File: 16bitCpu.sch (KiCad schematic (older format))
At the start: 0 parts

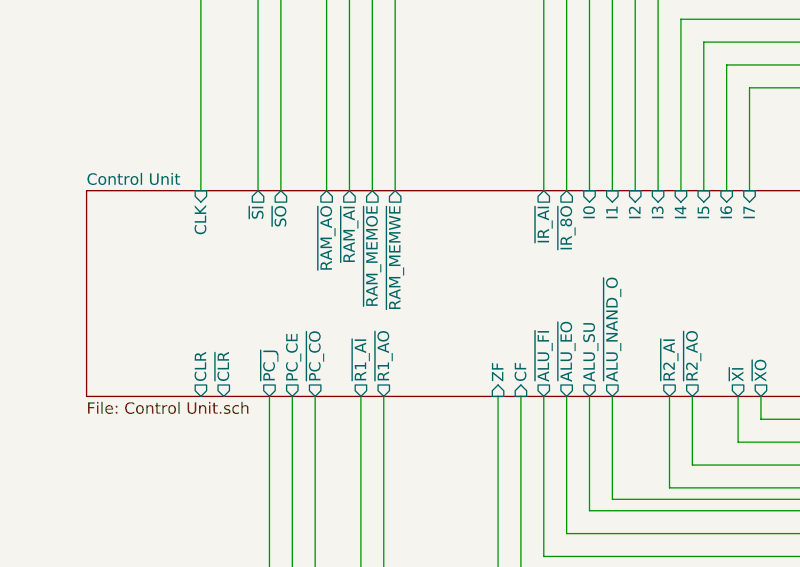
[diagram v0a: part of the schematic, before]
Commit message: using new RAM and ROM,15bits baby
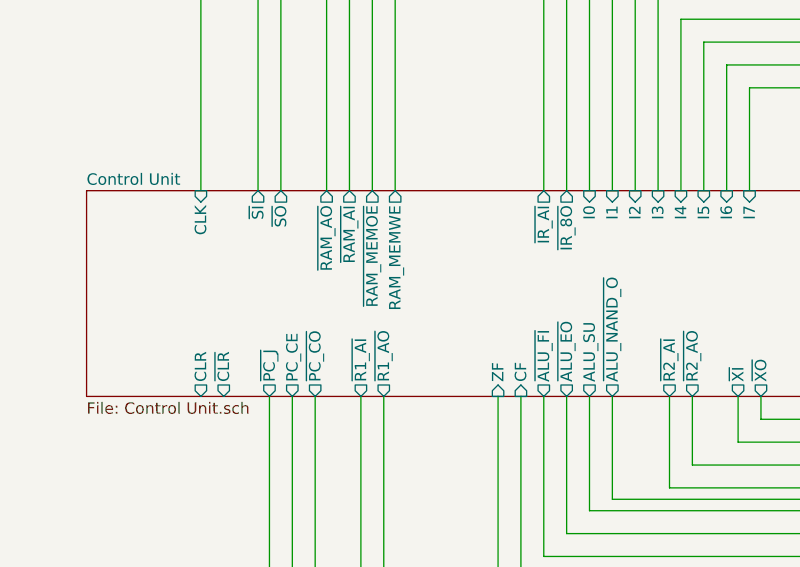
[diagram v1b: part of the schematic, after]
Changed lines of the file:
@@
 F21 "~RAM_AO" O T 1950 12300 50
 F22 "~RAM_MEMOE" O T 2150 12300 50
-F23 "~RAM_MEMWE" O T 2250 12300 50
-F24 "~IR_AI" O T 2900 12300 50
-F25 "~PC_J" O B 1700 13200 50
-F26 "PC_CE" O B 1800 13200 50
-F27 "~PC_CO" O B 1900 13200 50
-F28 "CLR" O B 1400 13200 50
-F29 "~CLR" O B 1500 13200 50
-F30 "~SI" O T 1650 12300 50
-F31 "~SO" O T 1750 12300 50
-F32 "~XI" O B 3750 13200 50
-F33 "~XO" O B 3850 13200 50
-F34 "~IR_8O" O T 3000 12300 50
-F35 "~ALU_NAND_O" O B 3200 13200 50
+F23 "~IR_AI" O T 2900 12300 50
+F24 "~PC_J" O B 1700 13200 50
+F25 "PC_CE" O B 1800 13200 50
+F26 "~PC_CO" O B 1900 13200 50
+F27 "CLR" O B 1400 13200 50
+F28 "~CLR" O B 1500 13200 50
+F29 "~SI" O T 1650 12300 50
+F30 "~SO" O T 1750 12300 50
+F31 "~XI" O B 3750 13200 50
+F32 "~XO" O B 3850 13200 50
+F33 "~IR_8O" O T 3000 12300 50
+F34 "~ALU_NAND_O" O B 3200 13200 50
+F35 "RAM_MEMWE" O T 2250 12300 50
 $EndSheet
 $Sheet

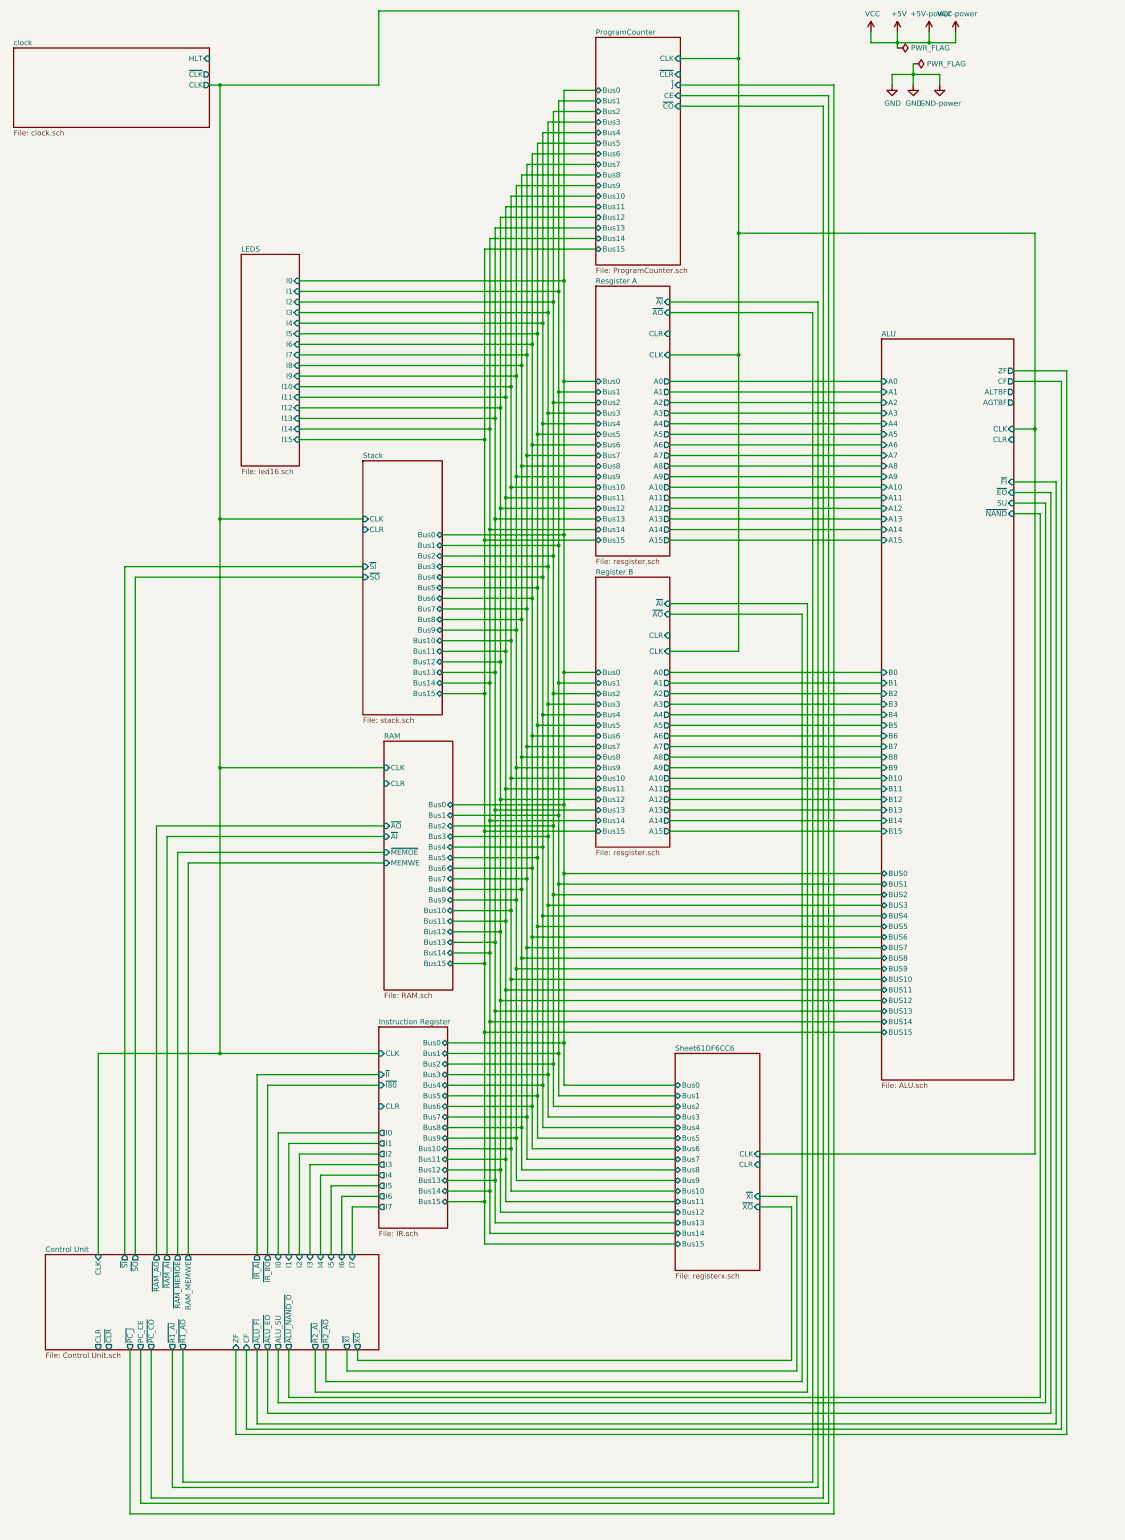
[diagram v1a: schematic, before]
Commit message: using new ROM in CU and more jumps
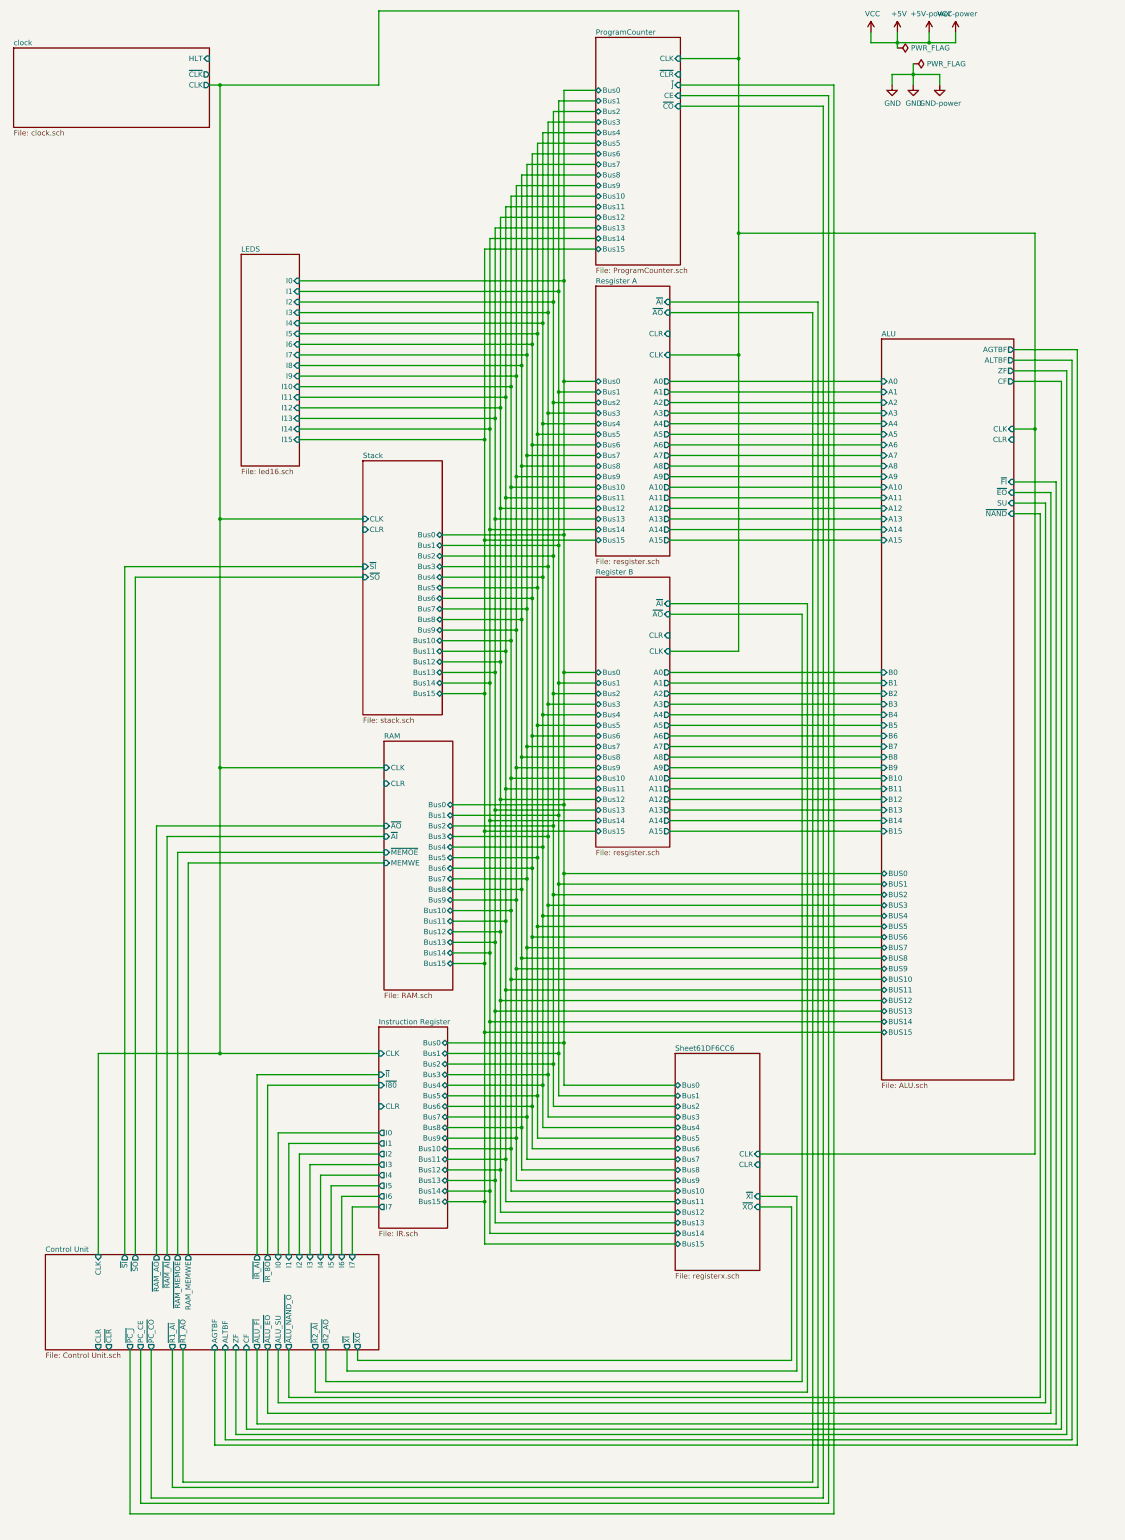
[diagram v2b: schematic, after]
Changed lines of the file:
@@
 F34 "~ALU_NAND_O" O B 3200 13200 50
 F35 "RAM_MEMWE" O T 2250 12300 50
+F36 "ALTBF" I B 2600 13200 50
+F37 "AGTBF" I B 2500 13200 50
 $EndSheet
 $Sheet
@@
 F55 "CF" O R 10050 4050 50
 F56 "ZF" O R 10050 3950 50
-F57 "ALTBF" O R 10050 4150 50
-F58 "AGTBF" O R 10050 4250 50
+F57 "ALTBF" O R 10050 3850 50
+F58 "AGTBF" O R 10050 3750 50
 F59 "~NAND" I R 10050 5300 50
 $EndSheet
@@
 Wire Wire Line
 	3200 13650 3200 13200
+Wire Wire Line
+	2600 13200 2600 14050
+Wire Wire Line
+	2600 14050 10600 14050
+Wire Wire Line
+	10600 14050 10600 3850
+Wire Wire Line
+	10600 3850 10050 3850
+Wire Wire Line
+	10050 3750 10650 3750
+Wire Wire Line
+	10650 3750 10650 14100
+Wire Wire Line
+	10650 14100 2500 14100
+Wire Wire Line
+	2500 14100 2500 13200
 $EndSCHEMATC

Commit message: fixed almost all errors
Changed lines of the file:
@@
 Wire Wire Line
 	7450 2650 10250 2650
-Wire Wire Line
-	10250 2650 10250 4500
 Connection ~ 7450 2650
 Wire Wire Line
@@
 Wire Wire Line
 	2500 14100 2500 13200
+Wire Wire Line
+	1400 13200 1400 14900
+Wire Wire Line
+	1400 14900 11000 14900
+Wire Wire Line
+	11000 4600 10050 4600
+Wire Wire Line
+	11000 1950 8500 1950
+Wire Wire Line
+	8500 1950 8500 1150
+Wire Wire Line
+	8500 1150 6900 1150
+Connection ~ 11000 4600
+Wire Wire Line
+	6800 6450 11000 6450
+Connection ~ 11000 6450
+Wire Wire Line
+	11000 6450 11000 4600
+Wire Wire Line
+	7650 11450 11000 11450
+Wire Wire Line
+	11000 6450 11000 11450
+Connection ~ 11000 11450
+Wire Wire Line
+	11000 11450 11000 14900
+Wire Wire Line
+	10250 2650 10250 4500
+Wire Wire Line
+	6800 3600 11000 3600
+Wire Wire Line
+	11000 1950 11000 3600
+Connection ~ 11000 3600
+Wire Wire Line
+	11000 3600 11000 4600
+Wire Wire Line
+	1400 14900 650  14900
+Wire Wire Line
+	650  5450 3900 5450
+Connection ~ 1400 14900
+Wire Wire Line
+	4100 7850 650  7850
+Connection ~ 650  7850
+Wire Wire Line
+	650  7850 650  5450
+Wire Wire Line
+	4050 10900 650  10900
+Wire Wire Line
+	650  7850 650  10900
+Connection ~ 650  10900
+Wire Wire Line
+	650  10900 650  14900
 $EndSCHEMATC

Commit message: fixed more errors
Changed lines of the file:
@@
 	8950 750  8950 850
-$Comp
-L 16bitCpu-rescue:PWR_FLAG-power #FLG01
-U 1 1 6041ADF9
-P 8950 900
-F 0 "#FLG01" H 8950 975 50  0001 C CNN
-F 1 "PWR_FLAG" V 8950 1028 50  0000 L CNN
-F 2 "" H 8950 900 50  0001 C CNN
-F 3 "~" H 8950 900 50  0001 C CNN
-	1    8950 900
-	0    1    1    0
-$EndComp
-$Comp
-L 16bitCpu-rescue:PWR_FLAG-power #FLG02
-U 1 1 6041B51D
-P 9100 1050
-F 0 "#FLG02" H 9100 1125 50  0001 C CNN
-F 1 "PWR_FLAG" V 9100 1178 50  0000 L CNN
-F 2 "" H 9100 1050 50  0001 C CNN
-F 3 "~" H 9100 1050 50  0001 C CNN
-	1    9100 1050
-	0    1    1    0
-$EndComp
 $Comp
 L 16bitCpu-rescue:GND-power #PWR04
@@
 	1    0    0    -1
 $EndComp
-Wire Wire Line
-	9100 1050 9100 1150
 $Comp
 L 16bitCpu-rescue:GND-power #PWR02
@@
 	8700 850  8950 850
 Connection ~ 8950 850
-Wire Wire Line
-	8950 850  8950 900
 $Sheet
 S 900  12300 3150 900

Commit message: added images,fixed readme,renamed stuff to not include spaces
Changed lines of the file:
@@
 S 6100 3150 700  2550
 U 5F67C726
-F0 "Resgister A" 50
+F0 "Resgister-A" 50
 F1 "resgister.sch" 50
 F2 "CLK" I R 6800 3800 50
@@
 S 6100 5900 700  2550
 U 5F74778C
-F0 "Register B" 50
+F0 "Register-B" 50
 F1 "resgister.sch" 50
 F2 "CLK" I R 6800 6600 50
@@
 Connection ~ 8950 850
 $Sheet
-S 900  12300 3150 900
-U 5FD099BF
-F0 "Control Unit" 50
-F1 "Control Unit.sch" 50
-F2 "I1" I T 3200 12300 50
-F3 "I0" I T 3100 12300 50
-F4 "I2" I T 3300 12300 50
-F5 "I3" I T 3400 12300 50
-F6 "I4" I T 3500 12300 50
-F7 "I5" I T 3600 12300 50
-F8 "I6" I T 3700 12300 50
-F9 "I7" I T 3800 12300 50
-F10 "CLK" I T 1400 12300 50
-F11 "ZF" I B 2700 13200 50
-F12 "CF" I B 2800 13200 50
-F13 "~ALU_FI" O B 2900 13200 50
-F14 "ALU_SU" O B 3100 13200 50
-F15 "~ALU_EO" O B 3000 13200 50
-F16 "~R1_AI" O B 2100 13200 50
-F17 "~R1_AO" O B 2200 13200 50
-F18 "~R2_AI" O B 3450 13200 50
-F19 "~R2_AO" O B 3550 13200 50
-F20 "~RAM_AI" O T 2050 12300 50
-F21 "~RAM_AO" O T 1950 12300 50
-F22 "~RAM_MEMOE" O T 2150 12300 50
-F23 "~IR_AI" O T 2900 12300 50
-F24 "~PC_J" O B 1700 13200 50
-F25 "PC_CE" O B 1800 13200 50
-F26 "~PC_CO" O B 1900 13200 50
-F27 "CLR" O B 1400 13200 50
-F28 "~CLR" O B 1500 13200 50
-F29 "~SI" O T 1650 12300 50
-F30 "~SO" O T 1750 12300 50
-F31 "~XI" O B 3750 13200 50
-F32 "~XO" O B 3850 13200 50
-F33 "~IR_8O" O T 3000 12300 50
-F34 "~ALU_NAND_O" O B 3200 13200 50
-F35 "RAM_MEMWE" O T 2250 12300 50
-F36 "ALTBF" I B 2600 13200 50
-F37 "AGTBF" I B 2500 13200 50
-$EndSheet
-$Sheet
 S 3900 4800 750  2400
 U 61968B9B
@@
 S 4050 10150 650  1900
 U 5F79B702
-F0 "Instruction Register" 50
+F0 "Instruction-Register" 50
 F1 "IR.sch" 50
 F2 "CLK" I L 4050 10400 50
@@
 Wire Wire Line
 	650  10900 650  14900
+$Sheet
+S 900  12300 3150 900
+U 5FD099BF
+F0 "Control-Unit" 50
+F1 "ControlUnit.sch" 50
+F2 "I1" I T 3200 12300 50
+F3 "I0" I T 3100 12300 50
+F4 "I2" I T 3300 12300 50
+F5 "I3" I T 3400 12300 50
+F6 "I4" I T 3500 12300 50
+F7 "I5" I T 3600 12300 50
+F8 "I6" I T 3700 12300 50
+F9 "I7" I T 3800 12300 50
+F10 "CLK" I T 1400 12300 50
+F11 "ZF" I B 2700 13200 50
+F12 "CF" I B 2800 13200 50
+F13 "~ALU_FI" O B 2900 13200 50
+F14 "ALU_SU" O B 3100 13200 50
+F15 "~ALU_EO" O B 3000 13200 50
+F16 "~R1_AI" O B 2100 13200 50
+F17 "~R1_AO" O B 2200 13200 50
+F18 "~R2_AI" O B 3450 13200 50
+F19 "~R2_AO" O B 3550 13200 50
+F20 "~RAM_AI" O T 2050 12300 50
+F21 "~RAM_AO" O T 1950 12300 50
+F22 "~RAM_MEMOE" O T 2150 12300 50
+F23 "~IR_AI" O T 2900 12300 50
+F24 "~PC_J" O B 1700 13200 50
+F25 "PC_CE" O B 1800 13200 50
+F26 "~PC_CO" O B 1900 13200 50
+F27 "CLR" O B 1400 13200 50
+F28 "~CLR" O B 1500 13200 50
+F29 "~SI" O T 1650 12300 50
+F30 "~SO" O T 1750 12300 50
+F31 "~XI" O B 3750 13200 50
+F32 "~XO" O B 3850 13200 50
+F33 "~IR_8O" O T 3000 12300 50
+F34 "~ALU_NAND_O" O B 3200 13200 50
+F35 "RAM_MEMWE" O T 2250 12300 50
+F36 "ALTBF" I B 2600 13200 50
+F37 "AGTBF" I B 2500 13200 50
+$EndSheet
 $EndSCHEMATC

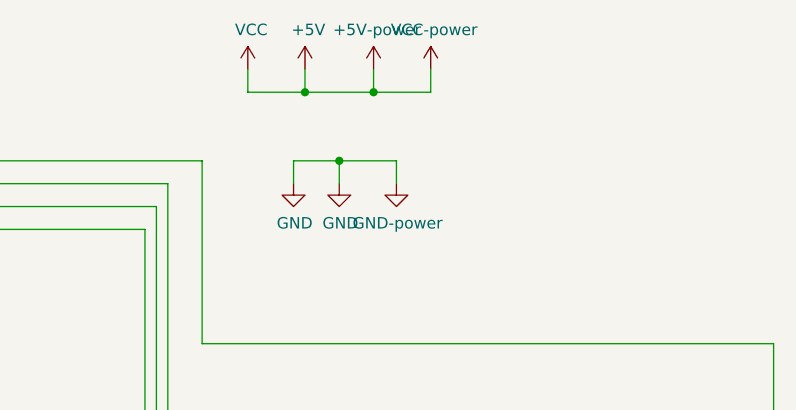
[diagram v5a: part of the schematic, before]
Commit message: Added power connector
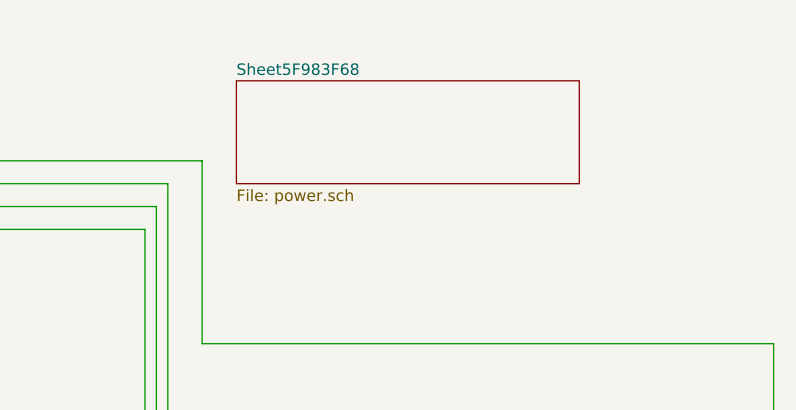
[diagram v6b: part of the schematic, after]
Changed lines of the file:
@@
 $Descr A3 11693 16535 portrait
 encoding utf-8
-Sheet 1 21
+Sheet 1 22
 Title ""
 Date ""
@@
 Wire Wire Line
 	5050 8300 6100 8300
-$Comp
-L 16bitCpu-rescue:+5V-power #PWR03
-U 1 1 603C06D7
-P 8950 750
-F 0 "#PWR03" H 8950 600 50  0001 C CNN
-F 1 "+5V" H 8965 923 50  0000 C CNN
-F 2 "" H 8950 750 50  0001 C CNN
-F 3 "" H 8950 750 50  0001 C CNN
-	1    8950 750
-	1    0    0    -1
-$EndComp
-Wire Wire Line
-	8950 750  8950 850
-$Comp
-L 16bitCpu-rescue:GND-power #PWR04
-U 1 1 6041B92E
-P 9100 1250
-F 0 "#PWR04" H 9100 1000 50  0001 C CNN
-F 1 "GND" H 9105 1077 50  0000 C CNN
-F 2 "" H 9100 1250 50  0001 C CNN
-F 3 "" H 9100 1250 50  0001 C CNN
-	1    9100 1250
-	1    0    0    -1
-$EndComp
-$Comp
-L 16bitCpu-rescue:GND-power #PWR02
-U 1 1 604BCEDD
-P 8900 1250
-F 0 "#PWR02" H 8900 1000 50  0001 C CNN
-F 1 "GND" H 8905 1077 50  0000 C CNN
-F 2 "" H 8900 1250 50  0001 C CNN
-F 3 "" H 8900 1250 50  0001 C CNN
-	1    8900 1250
-	1    0    0    -1
-$EndComp
-Wire Wire Line
-	8900 1250 8900 1150
-Wire Wire Line
-	8900 1150 9100 1150
-Connection ~ 9100 1150
-Wire Wire Line
-	9100 1150 9100 1250
-$Comp
-L 16bitCpu-rescue:VCC-power #PWR01
-U 1 1 604EB05F
-P 8700 750
-F 0 "#PWR01" H 8700 600 50  0001 C CNN
-F 1 "VCC" H 8715 923 50  0000 C CNN
-F 2 "" H 8700 750 50  0001 C CNN
-F 3 "" H 8700 750 50  0001 C CNN
-	1    8700 750
-	1    0    0    -1
-$EndComp
-Wire Wire Line
-	8700 750  8700 850
-Wire Wire Line
-	8700 850  8950 850
-Connection ~ 8950 850
 $Sheet
 S 3900 4800 750  2400
@@
 Wire Wire Line
 	4650 5500 5800 5500
-Wire Wire Line
-	8950 850  9250 850
-Wire Wire Line
-	9250 850  9250 750
-Wire Wire Line
-	9100 1150 9350 1150
-$Comp
-L 16bitCpu-rescue:GND-power #PWR06
-U 1 1 5FAE3C9B
-P 9350 1250
-F 0 "#PWR06" H 9350 1000 50  0001 C CNN
-F 1 "GND-power" H 9355 1077 50  0000 C CNN
-F 2 "" H 9350 1250 50  0001 C CNN
-F 3 "" H 9350 1250 50  0001 C CNN
-	1    9350 1250
-	1    0    0    -1
-$EndComp
-$Comp
-L 16bitCpu-rescue:+5V-power #PWR05
-U 1 1 5FAE3F33
-P 9250 750
-F 0 "#PWR05" H 9250 600 50  0001 C CNN
-F 1 "+5V-power" H 9265 923 50  0000 C CNN
-F 2 "" H 9250 750 50  0001 C CNN
-F 3 "" H 9250 750 50  0001 C CNN
-	1    9250 750
-	1    0    0    -1
-$EndComp
-Wire Wire Line
-	9250 850  9500 850
-Wire Wire Line
-	9500 850  9500 750
-Connection ~ 9250 850
-$Comp
-L 16bitCpu-rescue:VCC-power #PWR07
-U 1 1 5FB3A0D7
-P 9500 750
-F 0 "#PWR07" H 9500 600 50  0001 C CNN
-F 1 "VCC-power" H 9515 923 50  0000 C CNN
-F 2 "" H 9500 750 50  0001 C CNN
-F 3 "" H 9500 750 50  0001 C CNN
-	1    9500 750
-	1    0    0    -1
-$EndComp
 Wire Wire Line
 	6800 4050 8800 4050
@@
 Wire Wire Line
 	5600 11100 6850 11100
-Wire Wire Line
-	9350 1150 9350 1250
 $Sheet
 S 600  900  1850 750
@@
 F37 "AGTBF" I B 2500 13200 50
 $EndSheet
+$Sheet
+S 8650 800  1500 450
+U 5F983F69
+F0 "Sheet5F983F68" 50
+F1 "power.sch" 50
+$EndSheet
 $EndSCHEMATC
